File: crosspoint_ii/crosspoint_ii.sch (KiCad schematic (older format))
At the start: 1 part, among them P1 DIN_41612_128P

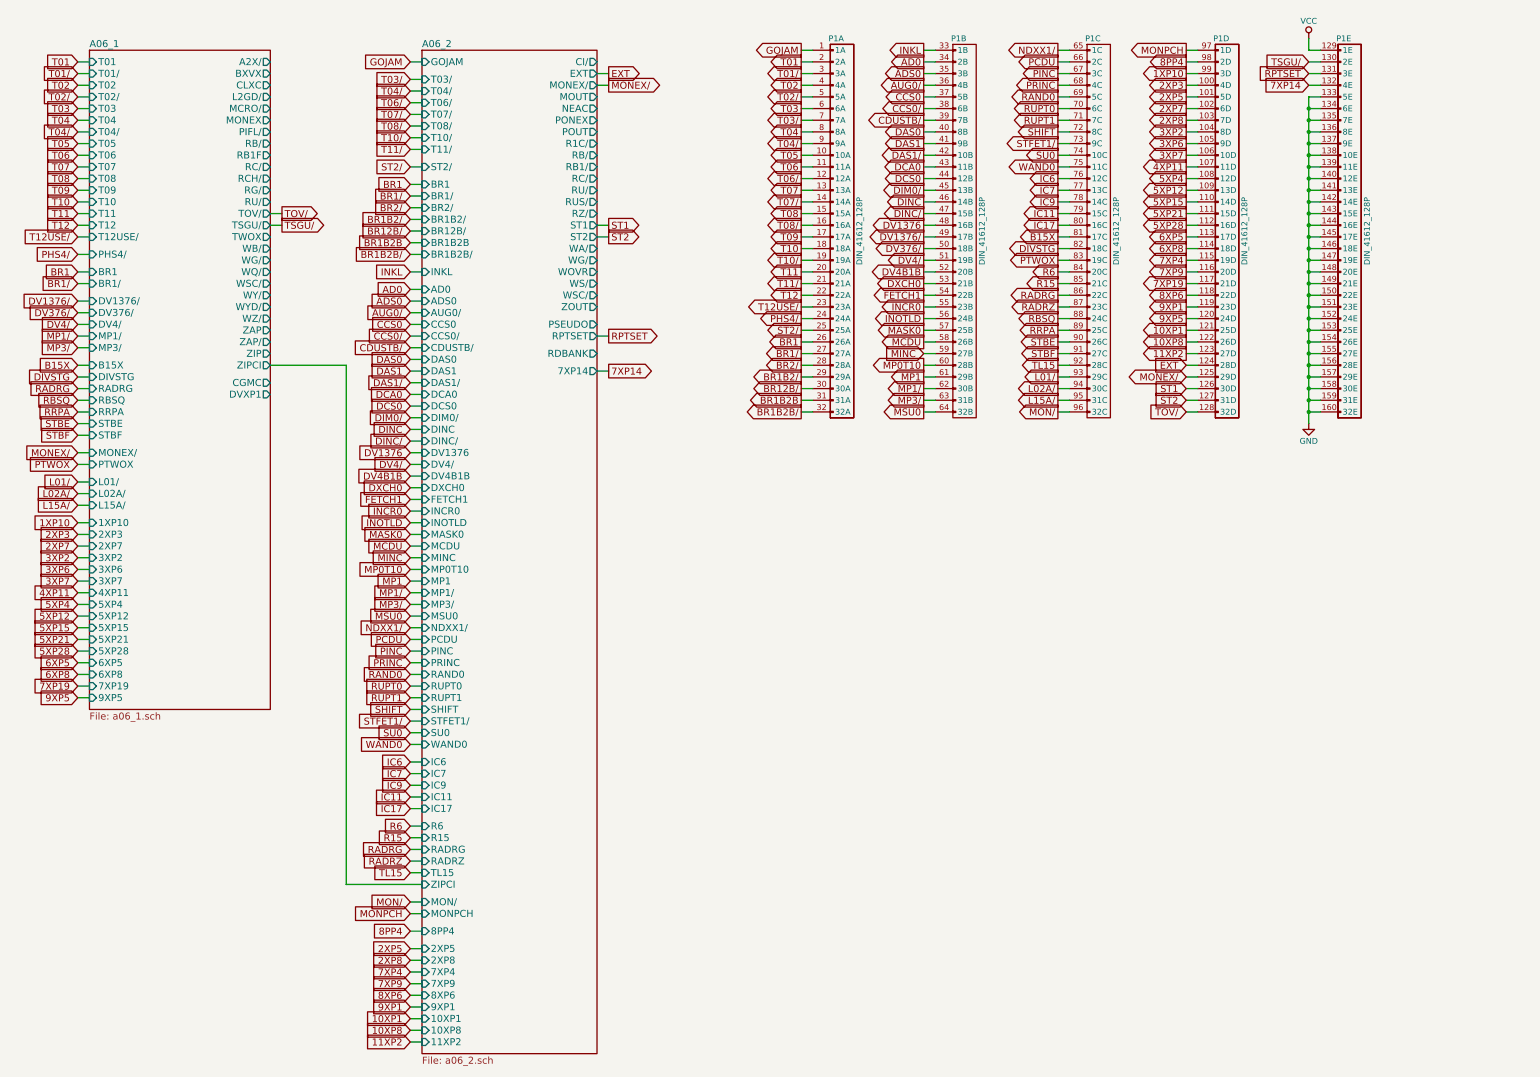
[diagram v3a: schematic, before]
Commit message: Tied in module 7, and corrected lots of errors.
Off the top of my head:
* T12DC/ not actually connected to restart logic in A02-2
* IC12/ and IC13 schematic errors
* Lots of gates moved from later modules up to modules 2-7
* YT0..7 logic dropped from 7, it belongs in 14
* Lots of missing signal breakouts
* ...probably some other things, I should keep a list as I go

All control pulses associated with GOJ1 now behave correctly during
GOJ1.
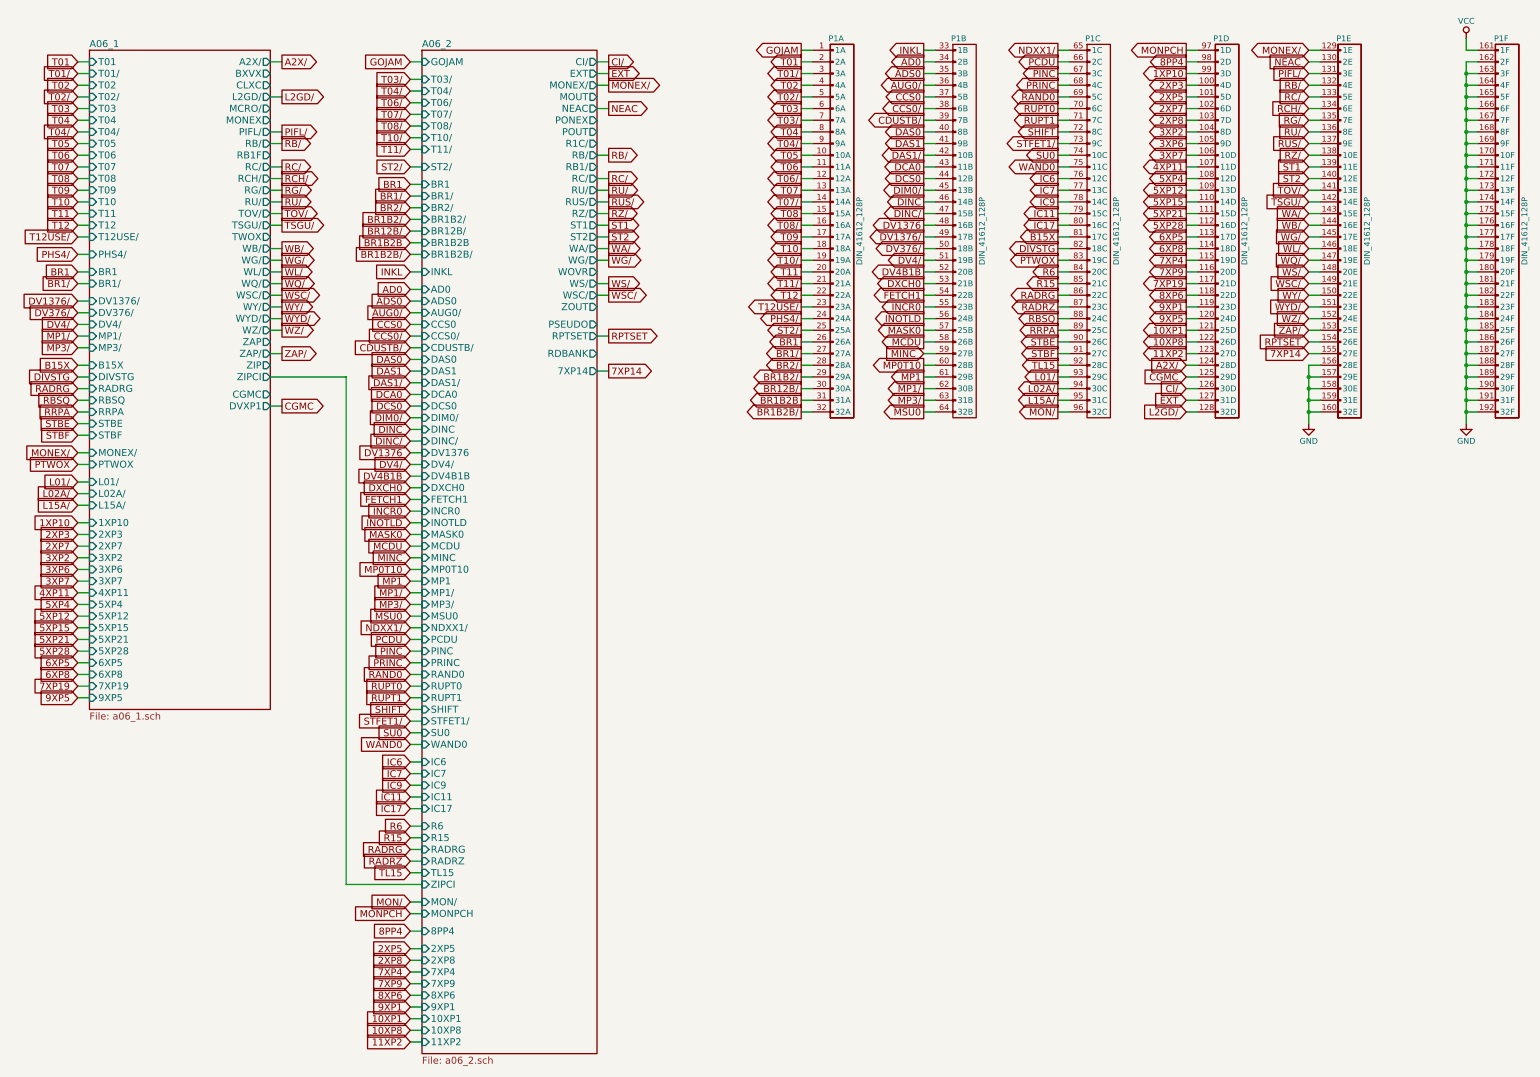
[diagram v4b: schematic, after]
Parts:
- added unit 6 of P1
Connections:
- net 7XP14: now also P1.155 (27E); no longer P1.132 (4E)
- net EXT: now also P1.127 (31D); no longer P1.124 (28D)
- net GND: now also P1.162 (2F), P1.163 (3F), P1.164 (4F), P1.165 (5F), P1.166 (6F), P1.167 (7F), P1.168 (8F), P1.169 (9F), P1.170 (10F), P1.171 (11F), P1.172 (12F), P1.173 (13F), P1.174 (14F), P1.175 (15F), P1.176 (16F), P1.177 (17F), P1.178 (18F), P1.179 (19F), P1.180 (20F), P1.181 (21F), P1.182 (22F), P1.183 (23F), P1.184 (24F), P1.185 (25F), P1.186 (26F), P1.187 (27F), P1.188 (28F), P1.189 (29F), P1.190 (30F), P1.191 (31F), P1.192 (32F); no longer P1.133 (5E), P1.134 (6E), P1.135 (7E), P1.136 (8E), P1.137 (9E), P1.138 (10E), P1.139 (11E), P1.140 (12E), P1.141 (13E), P1.142 (14E), P1.143 (15E), P1.144 (16E), P1.145 (17E), P1.146 (18E), P1.147 (19E), P1.148 (20E), P1.149 (21E), P1.150 (22E), P1.151 (23E), P1.152 (24E), P1.153 (25E), P1.154 (26E), P1.155 (27E)
- net MONEX/: now also P1.129 (1E); no longer P1.125 (29D)
- net RPTSET: now also P1.154 (26E); no longer P1.131 (3E)
- net ST1: now also P1.139 (11E); no longer P1.126 (30D)
- net ST2: now also P1.140 (12E); no longer P1.127 (31D)
- net TOV/: now also P1.141 (13E); no longer P1.128 (32D)
- net TSGU/: now also P1.142 (14E); no longer P1.130 (2E)
- net VCC: now also P1.161 (1F); no longer P1.129 (1E)
- new net A2X/: P1.124 (28D)
- new net CGMC: P1.125 (29D)
- new net CI/: P1.126 (30D)
- new net L2GD/: P1.128 (32D)
- new net NEAC: P1.130 (2E)
- new net PIFL/: P1.131 (3E)
- new net RB/: P1.132 (4E)
- new net RC/: P1.133 (5E)
- new net RCH/: P1.134 (6E)
- new net RG/: P1.135 (7E)
- new net RU/: P1.136 (8E)
- new net RUS/: P1.137 (9E)
- new net RZ/: P1.138 (10E)
- new net WA/: P1.143 (15E)
- new net WB/: P1.144 (16E)
- new net WG/: P1.145 (17E)
- new net WL/: P1.146 (18E)
- new net WQ/: P1.147 (19E)
- new net WS/: P1.148 (20E)
- new net WSC/: P1.149 (21E)
- new net WY/: P1.150 (22E)
- new net WYD/: P1.151 (23E)
- new net WZ/: P1.152 (24E)
- new net ZAP/: P1.153 (25E)

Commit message: Tied in module 8, and corrected lots of initial conditions.
The registers and ALU appear to work now, with TC0 and STD2 shuffling things around correctly, and Z counting up as instructions execute.
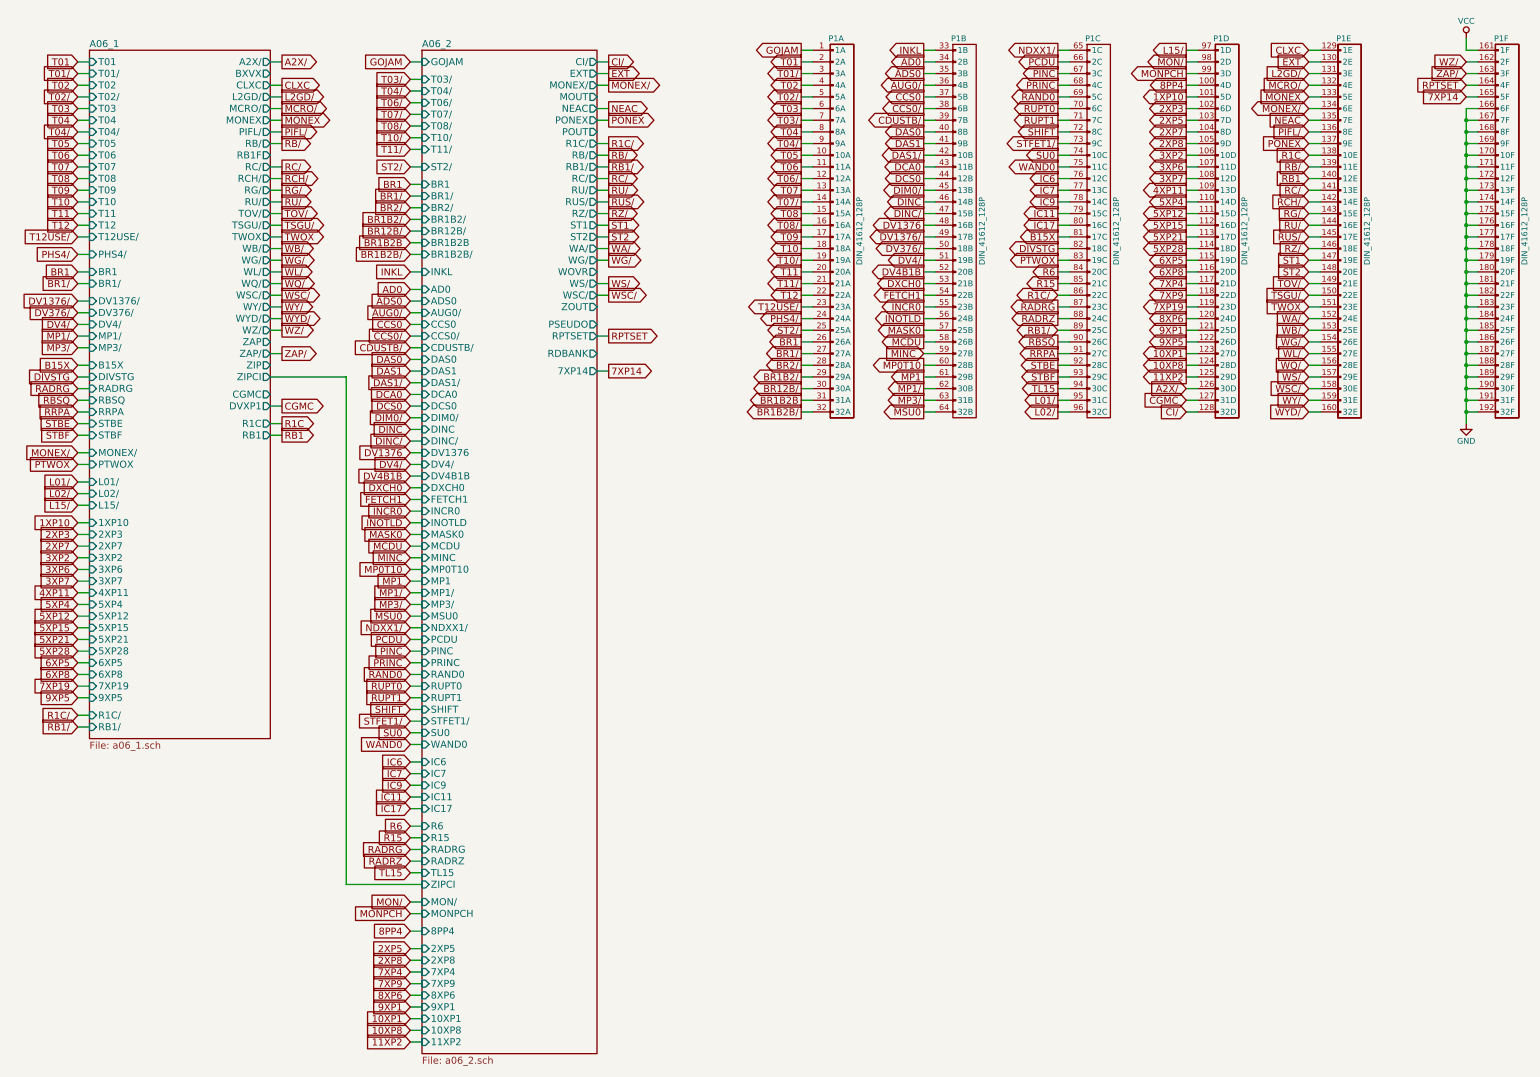
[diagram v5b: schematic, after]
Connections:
- net L02A/ is gone; now on net TL15: P1.94 (30C)
- net L15A/ is gone; now on net L01/: P1.95 (31C)
- net 10XP1: now also P1.123 (27D); no longer P1.121 (25D)
- net 10XP8: now also P1.124 (28D); no longer P1.122 (26D)
- net 11XP2: now also P1.125 (29D); no longer P1.123 (27D)
- net 1XP10: now also P1.101 (5D); no longer P1.99 (3D)
- net 2XP3: now also P1.102 (6D); no longer P1.100 (4D)
- net 2XP5: now also P1.103 (7D); no longer P1.101 (5D)
- net 2XP7: now also P1.104 (8D); no longer P1.102 (6D)
- net 2XP8: now also P1.105 (9D); no longer P1.103 (7D)
- net 3XP2: now also P1.106 (10D); no longer P1.104 (8D)
- net 3XP6: now also P1.107 (11D); no longer P1.105 (9D)
- net 3XP7: now also P1.108 (12D); no longer P1.106 (10D)
- net 4XP11: now also P1.109 (13D); no longer P1.107 (11D)
- net 5XP12: now also P1.111 (15D); no longer P1.109 (13D)
- net 5XP15: now also P1.112 (16D); no longer P1.110 (14D)
- net 5XP21: now also P1.113 (17D); no longer P1.111 (15D)
- net 5XP28: now also P1.114 (18D); no longer P1.112 (16D)
- net 5XP4: now also P1.110 (14D); no longer P1.108 (12D)
- net 6XP5: now also P1.115 (19D); no longer P1.113 (17D)
- net 6XP8: now also P1.116 (20D); no longer P1.114 (18D)
- net 7XP14: now also P1.165 (5F); no longer P1.155 (27E)
- net 7XP19: now also P1.119 (23D); no longer P1.117 (21D)
- net 7XP4: now also P1.117 (21D); no longer P1.115 (19D)
- net 7XP9: now also P1.118 (22D); no longer P1.116 (20D)
- net 8PP4: now also P1.100 (4D); no longer P1.98 (2D)
- net 8XP6: now also P1.120 (24D); no longer P1.118 (22D)
- net 9XP1: now also P1.121 (25D); no longer P1.119 (23D)
- net 9XP5: now also P1.122 (26D); no longer P1.120 (24D)
- net A2X/: now also P1.126 (30D); no longer P1.124 (28D)
- net CGMC: now also P1.127 (31D); no longer P1.125 (29D)
- net CI/: now also P1.128 (32D); no longer P1.126 (30D)
- net EXT: now also P1.130 (2E); no longer P1.127 (31D)
- net GND: no longer P1.156 (28E), P1.157 (29E), P1.158 (30E), P1.159 (31E), P1.160 (32E), P1.162 (2F), P1.163 (3F), P1.164 (4F), P1.165 (5F)
- net L01/: no longer P1.93 (29C)
- net L2GD/: now also P1.131 (3E); no longer P1.128 (32D)
- net MON/: now also P1.98 (2D); no longer P1.96 (32C)
- net MONEX/: now also P1.134 (6E); no longer P1.129 (1E)
- net MONPCH: now also P1.99 (3D); no longer P1.97 (1D)
- net NEAC: now also P1.135 (7E); no longer P1.130 (2E)
- net PIFL/: now also P1.136 (8E); no longer P1.131 (3E)
- net RADRG: now also P1.87 (23C); no longer P1.86 (22C)
- net RADRZ: now also P1.88 (24C); no longer P1.87 (23C)
- net RB/: now also P1.139 (11E); no longer P1.132 (4E)
- net RBSQ: now also P1.90 (26C); no longer P1.88 (24C)
- net RC/: now also P1.141 (13E); no longer P1.133 (5E)
- net RCH/: now also P1.142 (14E); no longer P1.134 (6E)
- net RG/: now also P1.143 (15E); no longer P1.135 (7E)
- net RPTSET: now also P1.164 (4F); no longer P1.154 (26E)
- net RRPA: now also P1.91 (27C); no longer P1.89 (25C)
- net RU/: now also P1.144 (16E); no longer P1.136 (8E)
- net RUS/: now also P1.145 (17E); no longer P1.137 (9E)
- net RZ/: now also P1.146 (18E); no longer P1.138 (10E)
- net ST1: now also P1.147 (19E); no longer P1.139 (11E)
- net ST2: now also P1.148 (20E); no longer P1.140 (12E)
- net STBE: now also P1.92 (28C); no longer P1.90 (26C)
- net STBF: now also P1.93 (29C); no longer P1.91 (27C)
- net TL15: no longer P1.92 (28C)
- net TOV/: now also P1.149 (21E); no longer P1.141 (13E)
- net TSGU/: now also P1.150 (22E); no longer P1.142 (14E)
- net WA/: now also P1.152 (24E); no longer P1.143 (15E)
- net WB/: now also P1.153 (25E); no longer P1.144 (16E)
- net WG/: now also P1.154 (26E); no longer P1.145 (17E)
- net WL/: now also P1.155 (27E); no longer P1.146 (18E)
- net WQ/: now also P1.156 (28E); no longer P1.147 (19E)
- net WS/: now also P1.157 (29E); no longer P1.148 (20E)
- net WSC/: now also P1.158 (30E); no longer P1.149 (21E)
- net WY/: now also P1.159 (31E); no longer P1.150 (22E)
- net WYD/: now also P1.160 (32E); no longer P1.151 (23E)
- net WZ/: now also P1.162 (2F); no longer P1.152 (24E)
- net ZAP/: now also P1.163 (3F); no longer P1.153 (25E)
- new net CLXC: P1.129 (1E)
- new net L02/: P1.96 (32C)
- new net L15/: P1.97 (1D)
- new net MCRO/: P1.132 (4E)
- new net MONEX: P1.133 (5E)
- new net PONEX: P1.137 (9E)
- new net R1C: P1.138 (10E)
- new net R1C/: P1.86 (22C)
- new net RB1: P1.140 (12E)
- new net RB1/: P1.89 (25C)
- new net TWOX: P1.151 (23E)
